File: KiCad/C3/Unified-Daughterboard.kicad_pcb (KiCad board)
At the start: 2 copper layers, 30 x 16.5 mm, 30 parts, among them J1 TYPE-C-31-M12_13, J3 Battery, J4 Conn_01x06, Q1 2N7002, SW1 PWR, U1 TPD4E05U06DQAR, U2 BQ24075

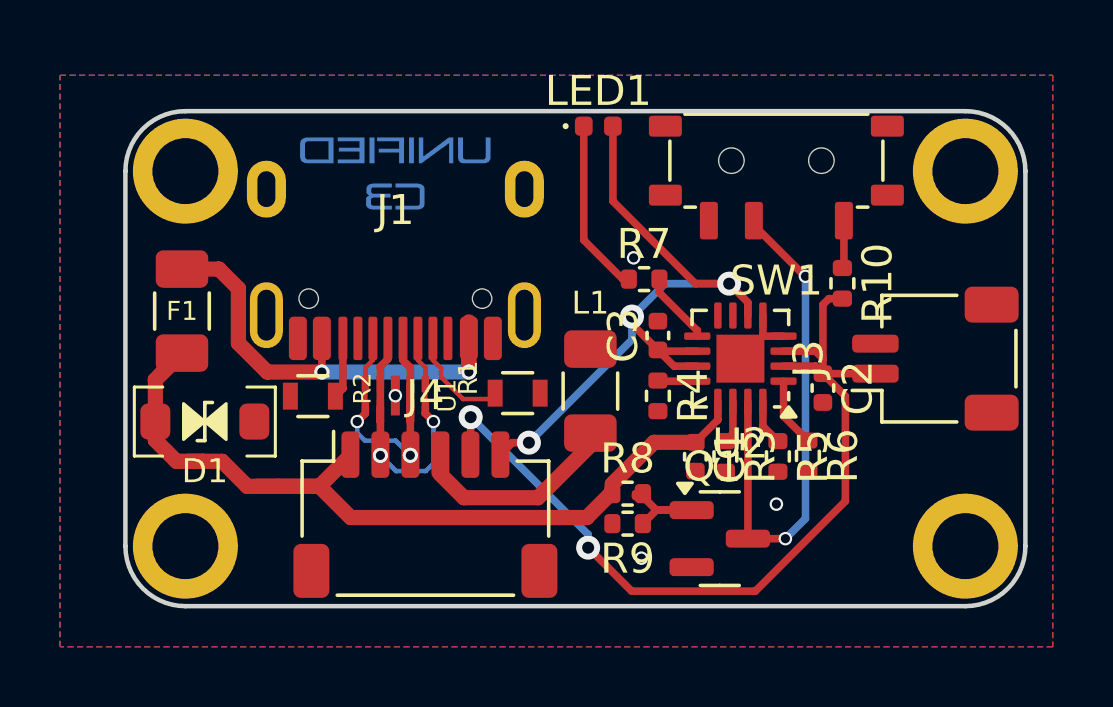
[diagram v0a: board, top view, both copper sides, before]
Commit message: STEP export
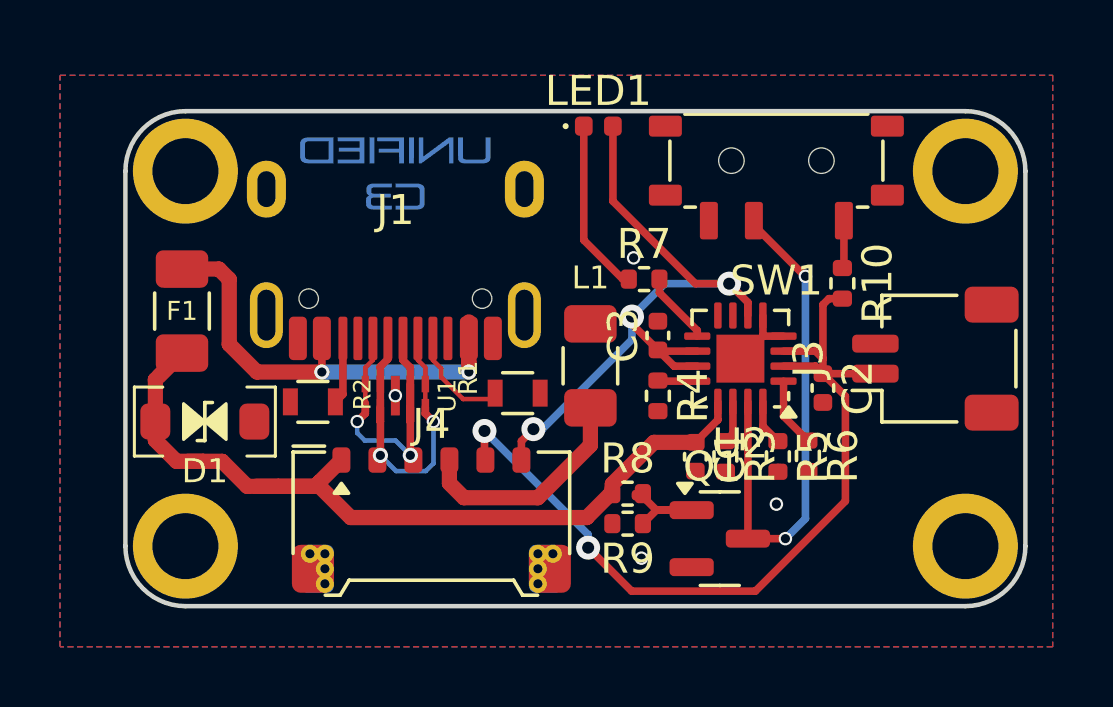
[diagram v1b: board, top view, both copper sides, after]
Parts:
- J4: footprint Connector_JST:JST_SH_SM06B-SRSS-TB_1x06-1MP_P1.00mm_Horizontal -> PCM_marbastlib-various:Molex_Pico-EZmate_78171-5006_1x06-1MP_P1.20mm_Vertical
- moved L1 0.84 mm to (81.5, 65.0)
- moved J4 0.21 mm to (76.2, 70.0)
- moved R2 0.19 mm to (72.3, 66.2)
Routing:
- net +BATT: track 29.8 -> 28.9 mm
- net GND: track 7.08 -> 7.65 mm
- net DA-: track 13.4 -> 13.9 mm
